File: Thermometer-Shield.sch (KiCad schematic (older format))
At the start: 48 parts, among them J1 CONN_01X04, J2 CONN_01X02, J3 CONN_01X02, J4 CONN_01X02, J5 CONN_01X02, Q1 Q_NPN_BCE, Q2 Q_NPN_BCE, Q3 Q_NPN_BCE, Q4 Q_NPN_BCE, Q5 Q_NPN_BCE, Q6 Q_NPN_BCE, Q7 Q_NPN_BCE, Q8 Q_NPN_BCE, SW1 SW_SPST, SW2 SW_SPST, SW3 SW_SPST, SW4 SW_SPST

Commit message: added documetation of parts, and some rework for more features
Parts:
- removed D1, D2, D3, D4: D, Diodes_THT:D_A-405_P7.62mm_Horizontal, symbol D
- removed Q1, Q2, Q3, Q4, Q5, Q6, Q7, Q8: Q_NPN_BCE, TO_SOT_Packages_THT:TO-92_Inline_Narrow_Oval, symbol Q_NPN_BCE
- removed R10, R11, R12, R13, R14, R15, R9: R, Resistors_THT:R_Axial_DIN0207_L6.3mm_D2.5mm_P10.16mm_Horizontal, symbol R
- added R17: 330, Resistors_SMD:R_0805_HandSoldering, symbol R
- added U1: ULN2803A, Housings_SOIC:SOIC-18W_7.5x11.6mm_Pitch1.27mm, symbol ULN2803A
- R0, R1, R2, R3, R4, R5, R6, R7, R8: value R -> 330
- R10: renamed from R18; value R -> 2K2; footprint Resistors_THT:R_Axial_DIN0207_L6.3mm_D2.5mm_P10.16mm_Horizontal -> Resistors_SMD:R_0805_HandSoldering
- R11: renamed from R19; value R -> 2K2; footprint Resistors_THT:R_Axial_DIN0207_L6.3mm_D2.5mm_P10.16mm_Horizontal -> Resistors_SMD:R_0805_HandSoldering
- R12: renamed from R20; value R -> 2K2; footprint Resistors_THT:R_Axial_DIN0207_L6.3mm_D2.5mm_P10.16mm_Horizontal -> Resistors_SMD:R_0805_HandSoldering
- R13: renamed from R21; value R -> 2K2; footprint Resistors_THT:R_Axial_DIN0207_L6.3mm_D2.5mm_P10.16mm_Horizontal -> Resistors_SMD:R_0805_HandSoldering
- R14: renamed from R22; value R -> 2K2; footprint Resistors_THT:R_Axial_DIN0207_L6.3mm_D2.5mm_P10.16mm_Horizontal -> Resistors_SMD:R_0805_HandSoldering
- R16: value R -> 330; footprint Resistors_THT:R_Axial_DIN0207_L6.3mm_D2.5mm_P10.16mm_Horizontal -> Resistors_SMD:R_0805_HandSoldering
- R18: renamed from R24; value R -> 2K2; footprint Resistors_THT:R_Axial_DIN0207_L6.3mm_D2.5mm_P10.16mm_Horizontal -> Resistors_SMD:R_0805_HandSoldering
- R9: renamed from R17; value R -> 2K2; footprint Resistors_THT:R_Axial_DIN0207_L6.3mm_D2.5mm_P10.16mm_Horizontal -> Resistors_SMD:R_0805_HandSoldering
- renumbered R23 to R15
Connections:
- net labels added: Out-Gnd, Trig-A, Trig-B, Trig-C, Trig-D
- wire segments 59 -> 66
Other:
- moved on the sheet: Disp1, J1, J2, J3, J4, J5, R0, R1, R10, R11, R12, R13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

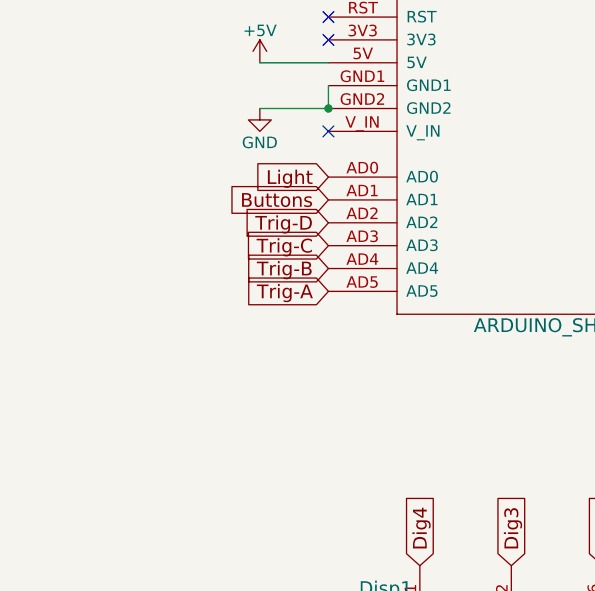
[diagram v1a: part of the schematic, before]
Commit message: added extension header with I2C layout
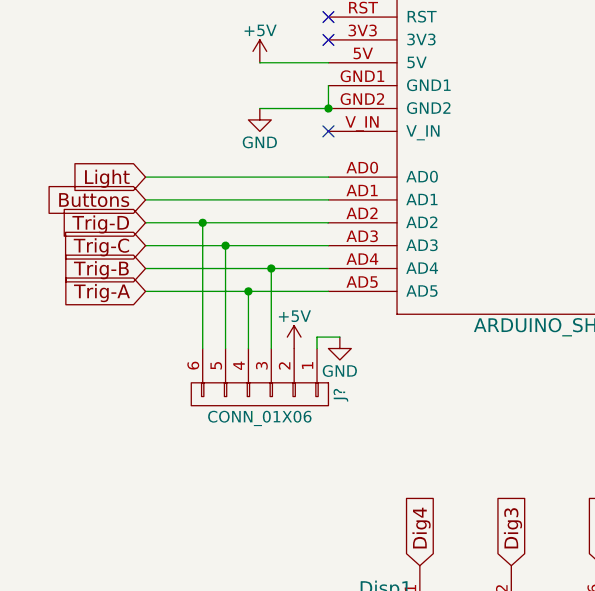
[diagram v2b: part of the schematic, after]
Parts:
- added J?: CONN_01X06, symbol CONN_01X06
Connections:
- net +5V: now also J?.2 (P2)
- net GND: now also J?.1 (P1)
- net Trig-A: now also J?.4 (P4)
- net Trig-B: now also J?.3 (P3)
- net Trig-C: now also J?.5 (P5)
- net Trig-D: now also J?.6 (P6)
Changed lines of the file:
@@
 Text GLabel 8550 5550 0    60   Input ~ 0
 Temp-Data
-Text GLabel 1750 3950 0    60   Input ~ 0
+Text GLabel 950  3950 0    60   Input ~ 0
 Light
-Text GLabel 1750 4050 0    60   Input ~ 0
+Text GLabel 950  4050 0    60   Input ~ 0
 Buttons
-Text GLabel 1750 4250 0    60   Input ~ 0
+Text GLabel 950  4250 0    60   Input ~ 0
 Trig-C
-Text GLabel 1750 4350 0    60   Input ~ 0
+Text GLabel 950  4350 0    60   Input ~ 0
 Trig-B
-Text GLabel 1750 4450 0    60   Input ~ 0
+Text GLabel 950  4450 0    60   Input ~ 0
 Trig-A
 Text GLabel 3650 3050 2    60   Input ~ 0
@@
 	1    0    0    -1
 $EndComp
-Text GLabel 1750 4150 0    60   Input ~ 0
+Text GLabel 950  4150 0    60   Input ~ 0
 Trig-D
 $Comp
@@
 Text Label 7050 4100 0    60   ~ 0
 Out-Gnd
+Wire Wire Line
+	950  3950 1750 3950
+Wire Wire Line
+	1750 4050 950  4050
+Wire Wire Line
+	950  4150 1750 4150
+Wire Wire Line
+	950  4250 1750 4250
+$Comp
+L CONN_01X06 J?
+U 1 1 594A71D7
+P 1450 4900
+F 0 "J?" H 1450 5250 50  0000 C CNN
+F 1 "CONN_01X06" V 1550 4900 50  0000 C CNN
+F 2 "" H 1450 4900 50  0001 C CNN
+F 3 "" H 1450 4900 50  0001 C CNN
+	1    1450 4900
+	0    1    1    0
+$EndComp
+Wire Wire Line
+	1300 4700 1300 4250
+Connection ~ 1300 4250
+Wire Wire Line
+	1200 4700 1200 4150
+Connection ~ 1200 4150
+$Comp
+L GND #PWR?
+U 1 1 594A7567
+P 1800 4650
+F 0 "#PWR?" H 1800 4400 50  0001 C CNN
+F 1 "GND" H 1800 4500 50  0000 C CNN
+F 2 "" H 1800 4650 50  0001 C CNN
+F 3 "" H 1800 4650 50  0001 C CNN
+	1    1800 4650
+	1    0    0    -1
+$EndComp
+$Comp
+L +5V #PWR?
+U 1 1 594A75DB
+P 1600 4700
+F 0 "#PWR?" H 1600 4550 50  0001 C CNN
+F 1 "+5V" H 1600 4840 50  0000 C CNN
+F 2 "" H 1600 4700 50  0001 C CNN
+F 3 "" H 1600 4700 50  0001 C CNN
+	1    1600 4700
+	1    0    0    -1
+$EndComp
+Wire Wire Line
+	1700 4700 1700 4650
+Wire Wire Line
+	1700 4650 1800 4650
+Wire Wire Line
+	950  4350 1750 4350
+Wire Wire Line
+	1750 4450 950  4450
+Wire Wire Line
+	1500 4700 1500 4350
+Connection ~ 1500 4350
+Wire Wire Line
+	1400 4700 1400 4450
+Connection ~ 1400 4450
 $EndSCHEMATC

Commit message: started reworking for shift register
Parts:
- removed R0, R16, R17: 330, Resistors_SMD:R_0805_HandSoldering, symbol R
- added R? (x2): 330, symbol R
- added U? (x2): 74HC595, symbol 74HC595
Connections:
- net +5V: no longer U1.10 (COM)
- net Dig1: now also U?.3 (QD); no longer SHIELD1.9
- net Dig2: now also U?.2 (QC); no longer SHIELD1.10
- net Dig3: now also U?.1 (QB); no longer SHIELD1.11
- net Dig4: now also U?.15 (QA); no longer SHIELD1.12
- net GND: now also U?.8 (GND), U?.8 (GND); no longer J2.2 (P2), J3.2 (P2), J4.2 (P2), J5.2 (P2)
- net Temp-Data: now also SHIELD1.2; no longer SHIELD1.13
- net at SHIELD1.1: no longer R1.2
- net at R2.2: now also U?.6 (QG); no longer SHIELD1.2
- net at SHIELD1.3: no longer R3.2
- net at SHIELD1.4: no longer R4.2
- net at SHIELD1.5: no longer R5.2
- net at SHIELD1.6: no longer R6.2
- net at SHIELD1.7: no longer R7.2
- net at SHIELD1.8: no longer R8.2
- net VCC: now reaches SHIELD1.V_IN
- net VCC: now also J2.2 (P2), J3.2 (P2), J4.2 (P2), J5.2 (P2), U1.10 (COM), U?.16 (VCC), U?.16 (VCC)
- net Degree: now reaches Disp1.12 (DEG-A)
- net Degree: now also R?.1
- net Extras: no longer names the net of Disp1.4 (DEG-C)
- net Extras: no longer Disp1.9 (COL-A)
- new net: R1.2, U?.7 (QH)
- new net: R3.2, U?.5 (QF)
- new net: R4.2, U?.4 (QE)
- new net: R5.2, U?.3 (QD)
- new net: R6.2, U?.2 (QC)
- new net: R7.2, U?.1 (QB)
- new net: R8.2, U?.15 (QA)
- new net: R?.2, U?.4 (QE)
- new net: R?.2, U?.5 (QF)
- new net Colon: Disp1.9 (COL-A), R?.1
- no-connect marks 5 -> 4
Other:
- moved on the sheet: J1, J2, J3, J4, J5, R1, R15, R18, R2, R3, R4, R5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

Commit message: schematic nearly done. PCB started
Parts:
- added J11: ShiftOut, Pin_Headers:Pin_Header_Straight_1x02_Pitch2.54mm, symbol CONN_01X02
- added J7: Out-E, Connectors:AK300-2, symbol CONN_01X02
- added J8: Out-F, Connectors:AK300-2, symbol CONN_01X02
- added JP1: CONN_02X02, Pin_Headers:Pin_Header_Straight_2x02_Pitch2.54mm, symbol CONN_02X02
- added O-A2, O-B2: out, Connectors:1pin, symbol CONN_01X01
- added Q1, Q2, Q3, Q4: Q_PNP_BCE, TO_SOT_Packages_THT:TO-92_Inline_Narrow_Oval, symbol Q_PNP_BCE
- added R19, R20, R21, R22: R, Resistors_SMD:R_0805_HandSoldering, symbol R
- J1: renamed from J?; value CONN_01X06 -> Analog/I2C; footprint (none) -> Pin_Headers:Pin_Header_Straight_1x06_Pitch2.54mm
- J2: renamed from J1; value CONN_01X04 -> TempSensor
- J3: renamed from J2; value CONN_01X02 -> Out-A
- J4: renamed from J3; value CONN_01X02 -> Out-B
- J5: renamed from J4; value CONN_01X02 -> Out-C
- J6: renamed from J5; value CONN_01X02 -> Out-D
- R10: renamed from R1; footprint Resistors_SMD:R_0805_HandSoldering -> Resistors_SMD:R_0603_HandSoldering
- R11, R12: renamed from R?; footprint (none) -> Resistors_SMD:R_0603_HandSoldering
- R3: renamed from R8; footprint Resistors_SMD:R_0805_HandSoldering -> Resistors_SMD:R_0603_HandSoldering
- R4: renamed from R7; footprint Resistors_SMD:R_0805_HandSoldering -> Resistors_SMD:R_0603_HandSoldering
- R5: renamed from R6; footprint Resistors_SMD:R_0805_HandSoldering -> Resistors_SMD:R_0603_HandSoldering
- R6: renamed from R5; footprint Resistors_SMD:R_0805_HandSoldering -> Resistors_SMD:R_0603_HandSoldering
- R7: renamed from R4; footprint Resistors_SMD:R_0805_HandSoldering -> Resistors_SMD:R_0603_HandSoldering
- R8: renamed from R3; footprint Resistors_SMD:R_0805_HandSoldering -> Resistors_SMD:R_0603_HandSoldering
- R9: renamed from R2; footprint Resistors_SMD:R_0805_HandSoldering -> Resistors_SMD:R_0603_HandSoldering
- U1, U2: renamed from U?; footprint (none) -> Housings_SSOP:TSSOP-16_4.4x5mm_Pitch0.65mm
- renumbered R15 to R1, R9 to R13, R10 to R14, R11 to R15, R12 to R16, R13 to R17, R14 to R18, R18 to R2, U1 to U3
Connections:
- net +5V: now also U1.10 (SRCLR), U2.10 (SRCLR), Q1.2 (C), Q2.2 (C), Q3.2 (C), Q4.2 (C)
- net A: now also R3.2, U1.4 (QE); no longer Disp1.14 (A), R7.1
- net B: now also R4.2, U1.5 (QF); no longer Disp1.16 (B), R8.1
- net C: now also R5.2, U1.6 (QG); no longer Disp1.13 (C), R9.1
- net Colon: now also U2.6 (QG); no longer Disp1.9 (COL-A)
- net D: now also R6.2, U1.1 (QB); no longer Disp1.3 (D), R4.1
- net DP: now also R10.2, U1.7 (QH); no longer Disp1.7 (DP), R10.1
- net Degree: now also U2.7 (QH); no longer Disp1.12 (DEG-A)
- net Dig1: now also Disp1.4 (DEG-C), Q1.3 (E); no longer U2.3 (QD)
- net Dig2: now also Disp1.10 (COL-C), Q2.3 (E); no longer U2.2 (QC)
- net Dig3: now also Q3.3 (E); no longer U2.1 (QB)
- net Dig4: now also Q4.3 (E); no longer U2.15 (QA)
- net E: now also R7.2, U1.15 (QA); no longer Disp1.5 (E), R3.1
- net F: now also R8.2, U1.3 (QD); no longer Disp1.11 (F), R6.1
- net G: now also R9.2, U1.2 (QC); no longer Disp1.15 (G), R5.1
- net GND: now also U1.13 (G), U2.13 (G)
- net Out-A: now also O-A2.1 (P1)
- net Out-B: now also O-B2.1 (P1)
- net Out-C: no longer U3.13 (O6)
- net Out-D: now also U3.13 (O6); no longer U3.11 (O8), U3.12 (O7)
- net Trig-A: now also SHIELD1.8, JP1.2 (P2); no longer J1.4 (P4), SHIELD1.AD5
- net Trig-B: now also SHIELD1.7, JP1.4 (P4); no longer J1.3 (P3), SHIELD1.AD4
- net Trig-C: now also SHIELD1.6; no longer J1.5 (P5), SHIELD1.AD3, U3.6 (I6)
- net Trig-D: now also SHIELD1.5, U3.6 (I6); no longer J1.6 (P6), SHIELD1.AD2, U3.7 (I7), U3.8 (I8)
- net VCC: now also J7.2 (P2), J8.2 (P2)
- net SS: now reaches SHIELD1.10
- net SS: now also U1.12 (RCLK), U2.12 (RCLK)
- net MOSI: now reaches SHIELD1.11
- net MOSI: now also U1.14 (SER)
- net at SHIELD1.12: now also JP1.1 (P1)
- net SCK: now reaches SHIELD1.13
- net SCK: now also U1.11 (SRCLK), U2.11 (SRCLK)
- net Trig-F: now reaches SHIELD1.3
- net Trig-F: now also U3.8 (I8)
- net Trig-E: now reaches SHIELD1.4
- net Trig-E: now also U3.7 (I7)
- net at SHIELD1.9: now also JP1.3 (P3)
- net at U1.9 (~QH): now also U2.14 (SER)
- net at R11.2: now also Disp1.9 (COL-A); no longer U2.4 (QE)
- net at R12.2: now also Disp1.12 (DEG-A); no longer U2.5 (QF)
- new net: J1.6 (P6), SHIELD1.AD2
- new net: J1.5 (P5), SHIELD1.AD3
- new net: J1.3 (P3), SHIELD1.AD4
- new net: J1.4 (P4), SHIELD1.AD5
- new net: Disp1.7 (DP), R10.1
- new net: Disp1.15 (G), R9.1
- new net: Disp1.11 (F), R8.1
- new net: Disp1.5 (E), R7.1
- new net: Disp1.3 (D), R6.1
- new net: Disp1.13 (C), R5.1
- new net: Disp1.16 (B), R4.1
- new net: Disp1.14 (A), R3.1
- new net: J11.2 (P2), U2.1 (QB)
- new net: J11.1 (P1), U2.15 (QA)
- new net: Q1.1 (B), R19.1
- new net: Q2.1 (B), R20.1
- new net: Q3.1 (B), R21.1
- new net: Q4.1 (B), R22.1
- new net Dig1_En: R19.2, U2.5 (QF)
- new net Dig2_En: R20.2, U2.4 (QE)
- new net Dig3_En: R21.2, U2.3 (QD)
- new net Dig4_En: R22.2, U2.2 (QC)
- new net Out-E: J7.1 (P1), U3.12 (O7)
- new net Out-F: J8.1 (P1), U3.11 (O8)
- no-connect marks 4 -> 7
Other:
- moved on the sheet: Disp1, J1, J2, J3, J4, J5, J6, R1, R10, R11, R12, R13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
